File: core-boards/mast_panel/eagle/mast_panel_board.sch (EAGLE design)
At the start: 36 parts, among them J1 2-PIN_2MM-V, J4 4-PIN_2MM-H, Q1 16MHz, U1 ATMEGA328P-AUR, U3 MCP2551T-I/SN, U4 MCP2515

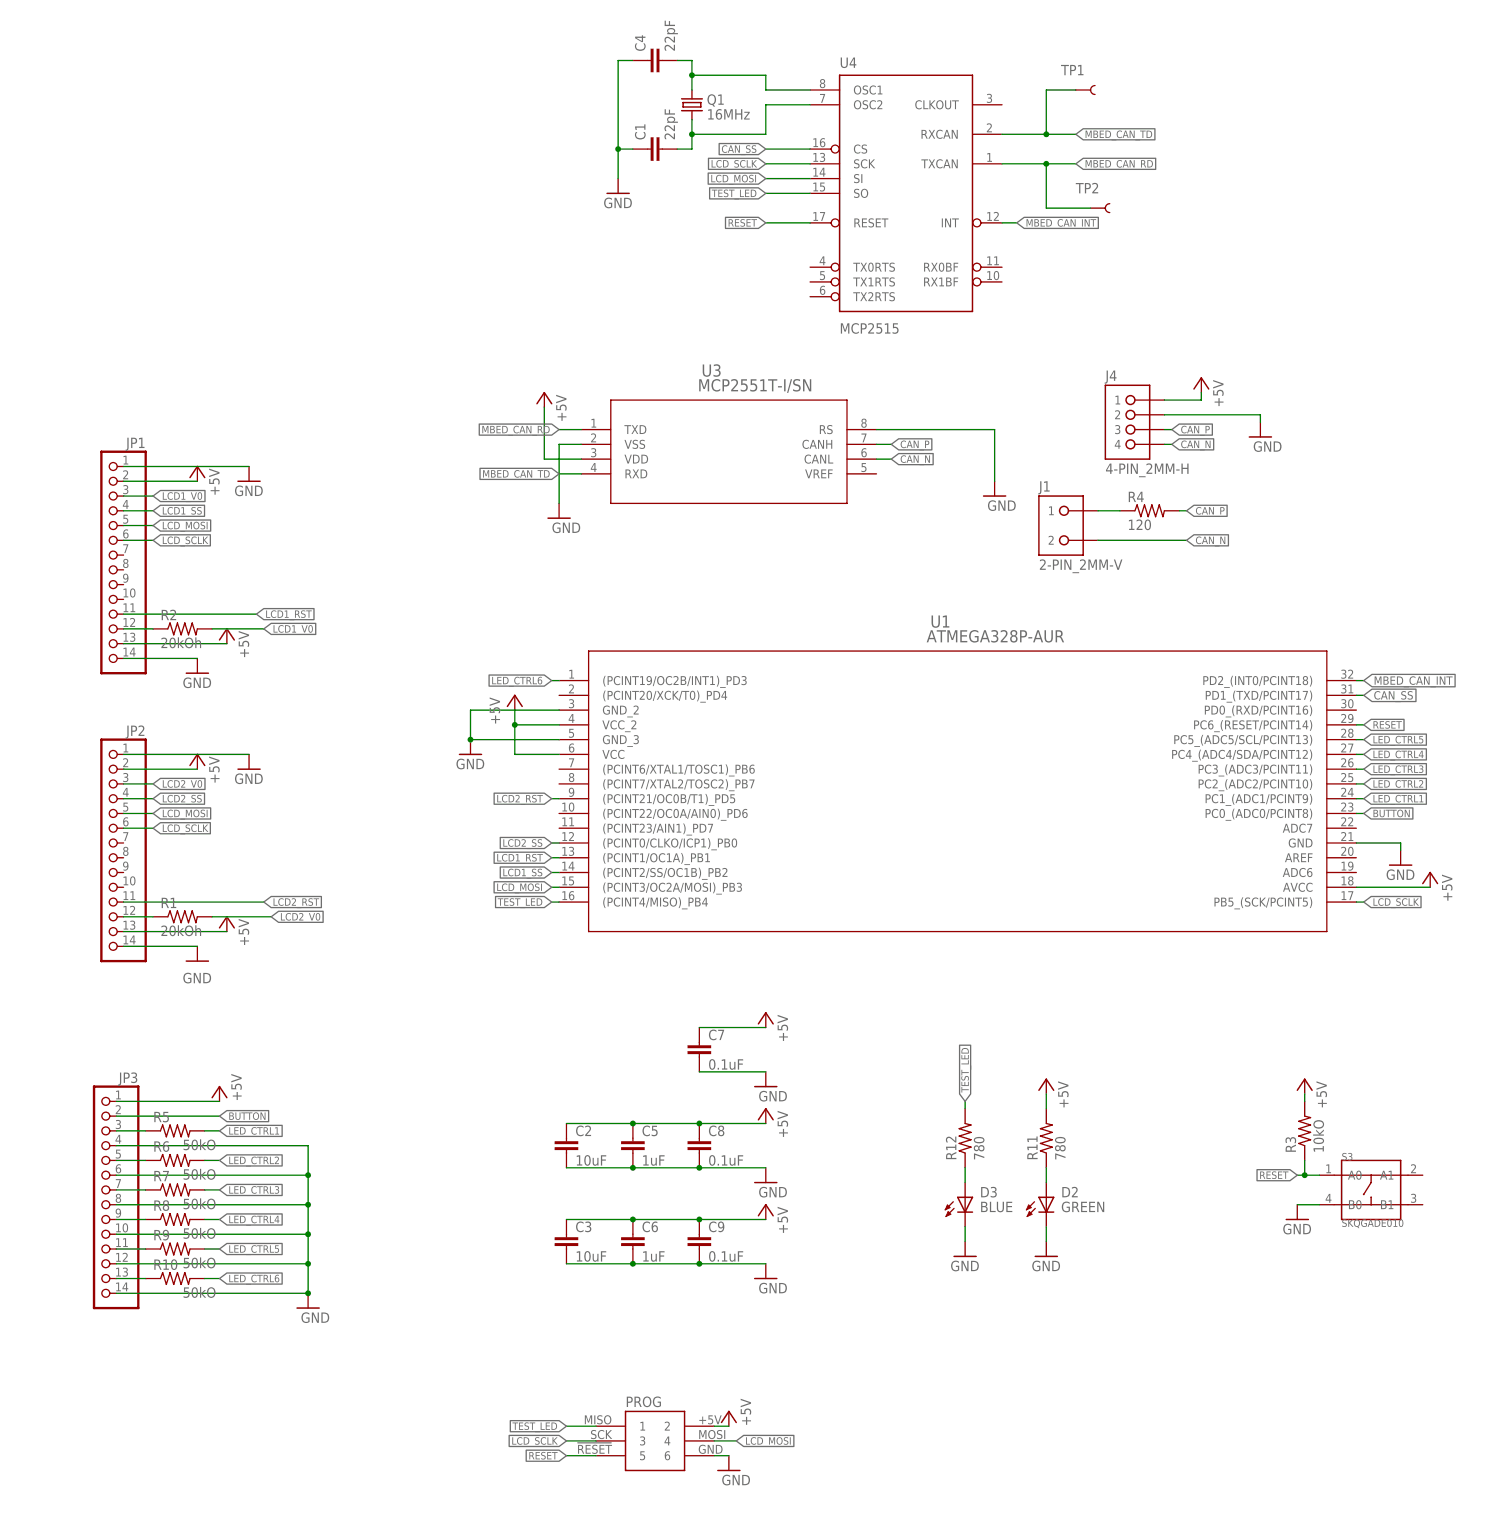
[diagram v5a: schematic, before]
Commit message: 4/14/20
Added CAN Controller
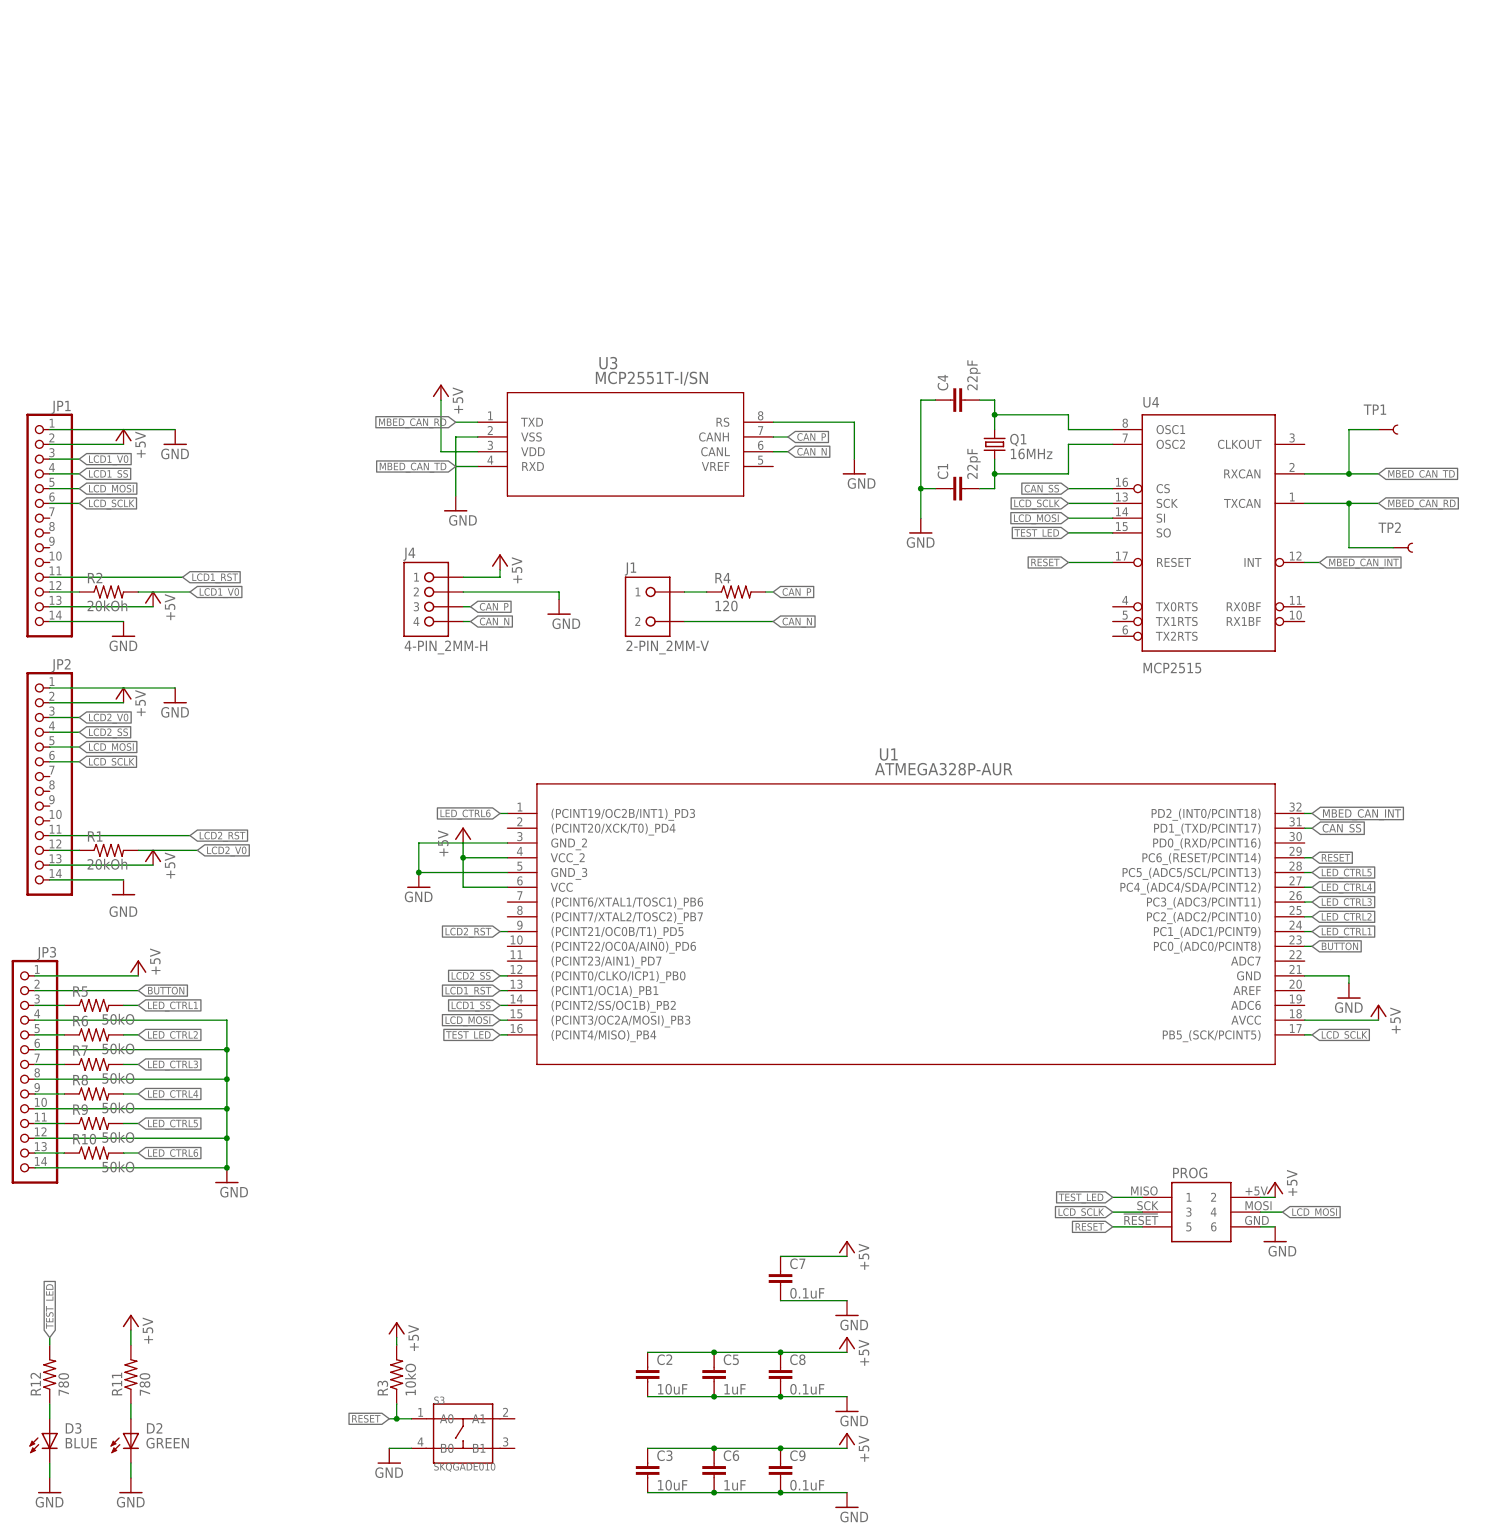
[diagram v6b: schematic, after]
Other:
- moved on the sheet: C1, C2, C3, C4, C5, C6, C7, C8, C9, D2, D3, J1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

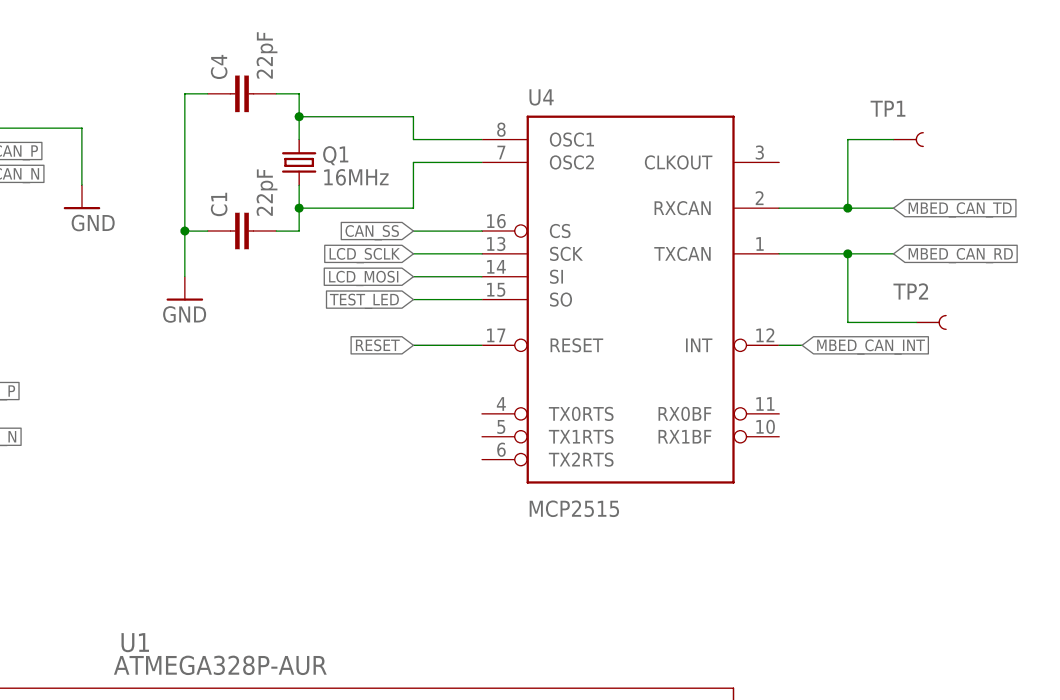
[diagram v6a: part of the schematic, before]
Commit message: 4/15/20
Touched up board
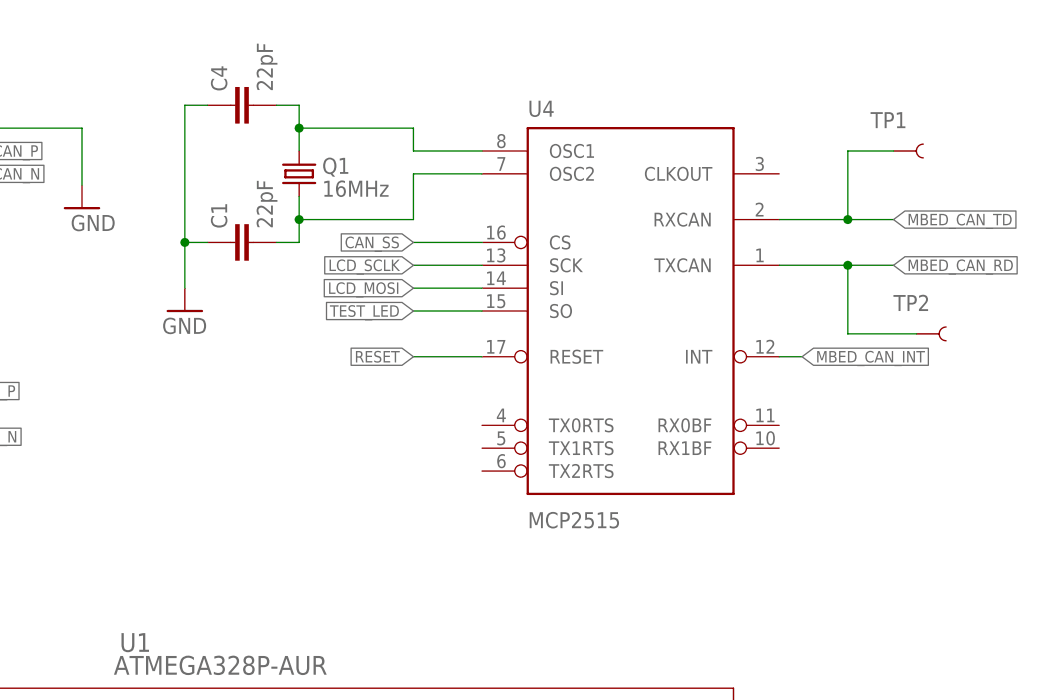
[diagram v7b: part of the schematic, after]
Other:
- note added: "CAN Controller"
- note added: "CAN Transceiver"
- note removed: "CAN Bus"
- moved on the sheet: C1, C4, Q1, TP1, TP2, U4
